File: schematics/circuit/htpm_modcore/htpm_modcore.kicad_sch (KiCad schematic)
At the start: 41 parts, among them J1 Conn_01x06_Pin, J10 Conn_01x04_Pin, J11 Conn_01x04_Pin, J12 Conn_01x04_Pin, J13 Conn_01x04_Pin, J14 Conn_01x15_Pin, J2 Conn_01x06_Pin, J3 Conn_01x06_Pin, J4 Conn_01x06_Pin, J5 Conn_01x02_Pin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

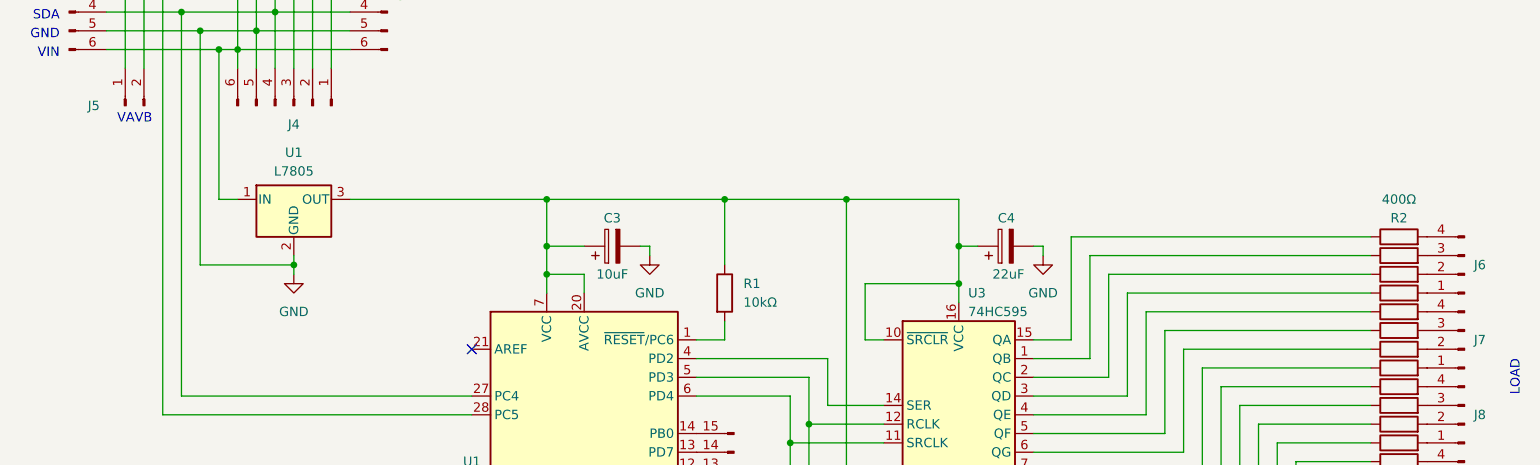
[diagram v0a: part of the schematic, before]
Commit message: Updated HTPm MODCORE nominal resistance values.
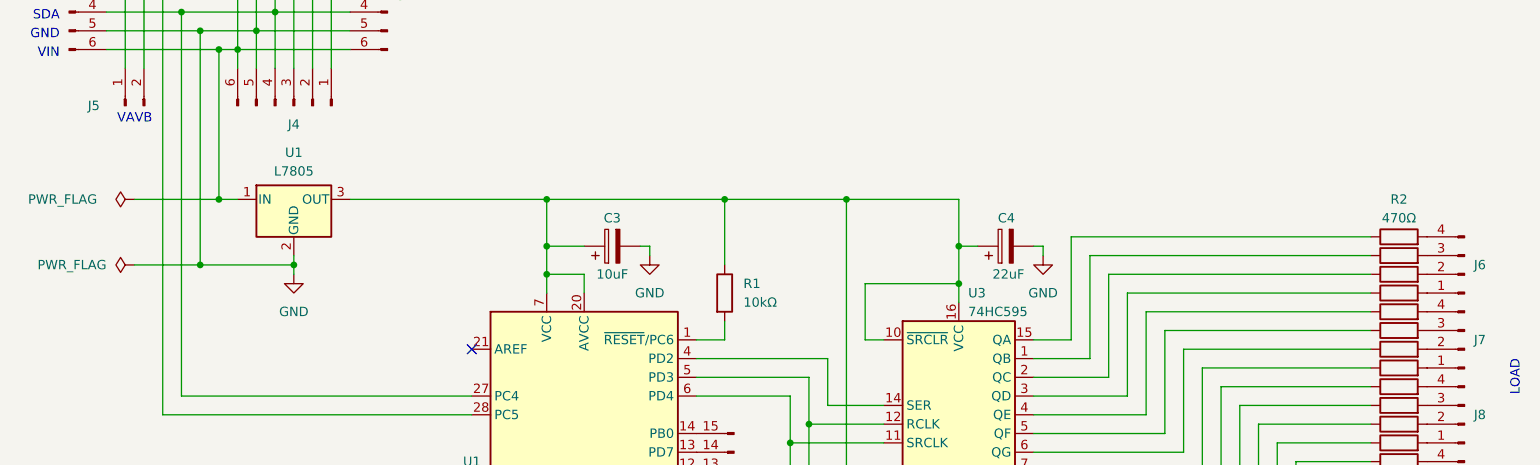
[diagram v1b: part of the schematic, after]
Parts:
- R10, R11, R12, R13, R14, R15, R16, R17, R2, R4, R5, R6, R7, R8, R9: value 400Ω -> 470Ω

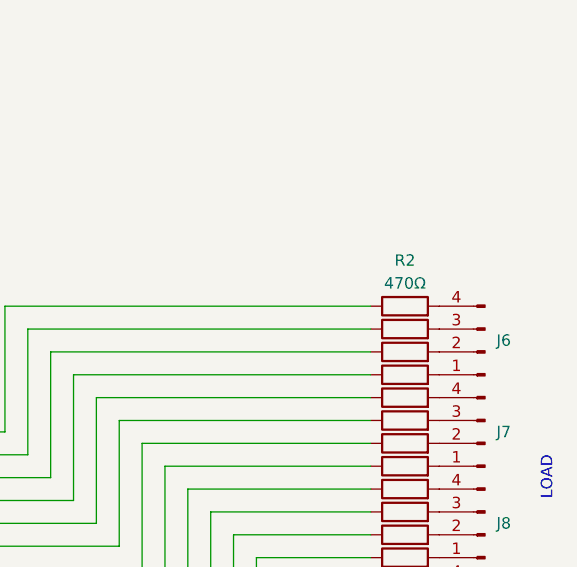
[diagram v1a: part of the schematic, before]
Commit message: Updated HTPm MODCORE nominal resistance values.
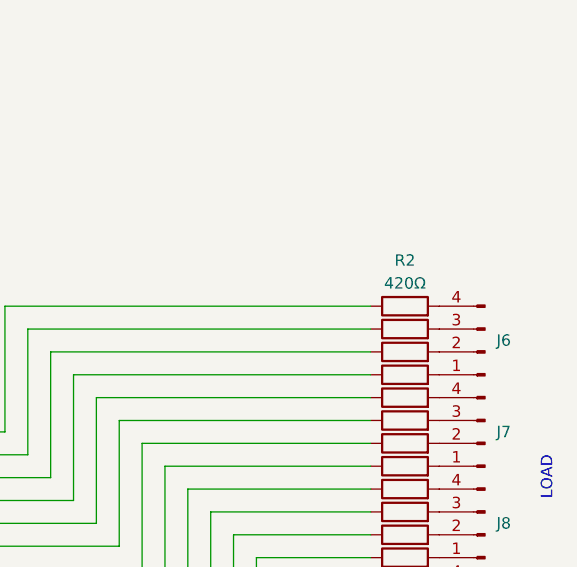
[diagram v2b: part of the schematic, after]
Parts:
- R10, R11, R12, R13, R14, R15, R16, R17, R2, R4, R5, R6, R7, R8, R9: value 470Ω -> 420Ω
- R3: value 400Ω -> 420Ω
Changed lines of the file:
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@@
       (effects (font (size 1.27 1.27)) hide)
     )
-    (property "Value" "470Ω" (at 214.63 69.85 90)
+    (property "Value" "420Ω" (at 214.63 69.85 90)
       (effects (font (size 1.27 1.27)) hide)
     )
@@
       (effects (font (size 1.27 1.27)) hide)
     )
-    (property "Value" "470Ω" (at 214.63 90.17 90)
+    (property "Value" "420Ω" (at 214.63 90.17 90)
       (effects (font (size 1.27 1.27)) hide)
     )
@@
       (effects (font (size 1.27 1.27)) hide)
     )
-    (property "Value" "470Ω" (at 214.63 72.39 90)
+    (property "Value" "420Ω" (at 214.63 72.39 90)
       (effects (font (size 1.27 1.27)) hide)
     )
@@
       (effects (font (size 1.27 1.27)) hide)
     )
-    (property "Value" "470Ω" (at 214.63 77.47 90)
+    (property "Value" "420Ω" (at 214.63 77.47 90)
       (effects (font (size 1.27 1.27)) hide)
     )
@@
       (effects (font (size 1.27 1.27)) hide)
     )
-    (property "Value" "470Ω" (at 214.63 87.63 90)
+    (property "Value" "420Ω" (at 214.63 87.63 90)
       (effects (font (size 1.27 1.27)) hide)
     )
@@
       (effects (font (size 1.27 1.27)) hide)
     )
-    (property "Value" "470Ω" (at 214.63 85.09 90)
+    (property "Value" "420Ω" (at 214.63 85.09 90)
       (effects (font (size 1.27 1.27)) hide)
     )
@@
       (effects (font (size 1.27 1.27)) hide)
     )
-    (property "Value" "470Ω" (at 214.63 64.77 90)
+    (property "Value" "420Ω" (at 214.63 64.77 90)
       (effects (font (size 1.27 1.27)) hide)
     )
@@
       (effects (font (size 1.27 1.27)))
     )
-    (property "Value" "470Ω" (at 214.63 60.96 90)
+    (property "Value" "420Ω" (at 214.63 60.96 90)
       (effects (font (size 1.27 1.27)))
     )
@@
       (effects (font (size 1.27 1.27)) hide)
     )
-    (property "Value" "470Ω" (at 214.63 95.25 90)
+    (property "Value" "420Ω" (at 214.63 95.25 90)
       (effects (font (size 1.27 1.27)) hide)
     )
@@
       (effects (font (size 1.27 1.27)) hide)
     )
-    (property "Value" "470Ω" (at 214.63 80.01 90)
+    (property "Value" "420Ω" (at 214.63 80.01 90)
       (effects (font (size 1.27 1.27)) hide)
     )
@@
       (effects (font (size 1.27 1.27)) hide)
     )
-    (property "Value" "400Ω" (at 214.63 62.23 90)
+    (property "Value" "420Ω" (at 214.63 62.23 90)
       (effects (font (size 1.27 1.27)) hide)
     )
@@
       (effects (font (size 1.27 1.27)) hide)
     )
-    (property "Value" "470Ω" (at 214.63 82.55 90)
+    (property "Value" "420Ω" (at 214.63 82.55 90)
       (effects (font (size 1.27 1.27)) hide)
     )
@@
       (effects (font (size 1.27 1.27)) hide)
     )
-    (property "Value" "470Ω" (at 214.63 92.71 90)
+    (property "Value" "420Ω" (at 214.63 92.71 90)
       (effects (font (size 1.27 1.27)) hide)
     )
@@
       (effects (font (size 1.27 1.27)) hide)
     )
-    (property "Value" "470Ω" (at 214.63 74.93 90)
+    (property "Value" "420Ω" (at 214.63 74.93 90)
       (effects (font (size 1.27 1.27)) hide)
     )
@@
       (effects (font (size 1.27 1.27)))
     )
-    (property "Value" "470Ω" (at 214.63 97.79 90)
+    (property "Value" "420Ω" (at 214.63 97.79 90)
       (effects (font (size 1.27 1.27)) hide)
     )
@@
       (effects (font (size 1.27 1.27)) hide)
     )
-    (property "Value" "470Ω" (at 214.63 67.31 90)
-      (effects (font (size 1.27 1.27)) hide)
-    )
+    (property "Value" "420Ω" (at 214.63 67.31 90)
+      (effects (font (size 1.27 1.27)) hide)
+    )
